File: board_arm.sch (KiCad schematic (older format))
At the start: 153 parts, among them SW1 SW_SPDT, U1 STM32F072CBT6, U2 PRTR5V0U2X, U3 MCP1725-3302E_SN

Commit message: Renumber the caps
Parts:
- renumbered C12 to C1, C1 to C3, C6 to C5, C7 to C6, C9 to C7, C10 to C8, C11 to C9
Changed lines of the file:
@@
 $EndDescr
 $Comp
-L Device:C_Small C1
+L Device:C_Small C3
 U 1 1 5C603E42
 P 1725 5275
-F 0 "C1" H 1817 5321 50  0000 L CNN
+F 0 "C3" H 1817 5321 50  0000 L CNN
 F 1 "0.1uF" H 1817 5230 50  0000 L CNN
 F 2 "Capacitor_SMD:C_0805_2012Metric" H 1725 5275 50  0001 C CNN
@@
 $EndComp
 $Comp
-L Device:C_Small C11
+L Device:C_Small C9
 U 1 1 5C9712E3
 P 7575 7200
-F 0 "C11" H 7667 7246 50  0000 L CNN
+F 0 "C9" H 7667 7246 50  0000 L CNN
 F 1 "10uF" H 7667 7155 50  0000 L CNN
 F 2 "Capacitor_SMD:C_0805_2012Metric" H 7575 7200 50  0001 C CNN
@@
 	5650 6700 5650 6600
 $Comp
-L Device:C_Small C9
+L Device:C_Small C7
 U 1 1 5CA16B93
 P 5425 6750
-F 0 "C9" H 5517 6796 50  0000 L CNN
+F 0 "C7" H 5517 6796 50  0000 L CNN
 F 1 "10uF" H 5517 6705 50  0000 L CNN
 F 2 "Capacitor_SMD:C_0805_2012Metric" H 5425 6750 50  0001 C CNN
@@
 	7950 6600 7950 6525
 $Comp
-L Device:C_Small C10
+L Device:C_Small C8
 U 1 1 5CA47771
 P 7150 7200
-F 0 "C10" H 7242 7246 50  0000 L CNN
+F 0 "C8" H 7242 7246 50  0000 L CNN
 F 1 "1nF" H 7242 7155 50  0000 L CNN
 F 2 "Capacitor_SMD:C_0805_2012Metric" H 7150 7200 50  0001 C CNN
@@
 PWRGD
 $Comp
-L Device:C_Small C6
+L Device:C_Small C5
 U 1 1 5D2621C9
 P 2525 5275
-F 0 "C6" H 2617 5321 50  0000 L CNN
+F 0 "C5" H 2617 5321 50  0000 L CNN
 F 1 "4.7uF" H 2617 5230 50  0000 L CNN
 F 2 "Capacitor_SMD:C_0805_2012Metric" H 2525 5275 50  0001 C CNN
@@
 $EndComp
 $Comp
-L Device:C_Small C7
+L Device:C_Small C6
 U 1 1 5D29FD29
 P 2925 5275
-F 0 "C7" H 3017 5321 50  0000 L CNN
+F 0 "C6" H 3017 5321 50  0000 L CNN
 F 1 "10nF" H 3017 5230 50  0000 L CNN
 F 2 "Capacitor_SMD:C_0805_2012Metric" H 2925 5275 50  0001 C CNN
@@
 NoConn ~ 2425 2625
 $Comp
-L Device:C_Small C12
+L Device:C_Small C1
 U 1 1 5C774367
 P 1950 1575
-F 0 "C12" H 2042 1621 50  0000 L CNN
+F 0 "C1" H 2042 1621 50  0000 L CNN
 F 1 "0.1uF" H 2042 1530 50  0000 L CNN
 F 2 "Capacitor_SMD:C_0805_2012Metric" H 1950 1575 50  0001 C CNN

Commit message: routage premiere version
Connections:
- net COL0: now also K_CAPS1.1 (COL), K_ESC1.1 (COL), K_SHIFT1.1 (COL), K_TAB1.1 (COL), U1.28 (PB15)
- net COL1: now also K_#1.1 (COL), K_A1.1 (COL), K_Q1.1 (COL), U1.27 (PB14)
- net COL10: now also K_#10.1 (COL), K_.1.1 (COL), K_;1.1 (COL), K_P1.1 (COL), U1.43 (PB7)
- net COL11: now also K_'1.1 (COL), K_-1.1 (COL), K_/1.1 (COL), K_[1.1 (COL), U1.42 (PB6)
- net COL12: now also K_=1.1 (COL), K_RSHIFT1.1 (COL), K_]1.1 (COL), U1.41 (PB5)
- net COL13: now also K_BACK1.1 (COL), K_ENTER1.1 (COL), K_\1.1 (COL), U1.39 (PB3)
- net COL14: now also K_UP1.1 (COL), U1.40 (PB4)
- net COL15: now also K_DELETE1.1 (COL), K_INSERT1.1 (COL), U1.18 (PB0)
- net COL2: now also K_#2.1 (COL), K_S1.1 (COL), K_W1.1 (COL), K_Z1.1 (COL), U1.26 (PB13)
- net COL3: now also K_#3.1 (COL), K_D1.1 (COL), K_E1.1 (COL), U1.25 (PB12)
- net COL4: now also K_#4.1 (COL), K_F1.1 (COL), K_R1.1 (COL), U1.22 (PB11)
- net COL5: now also K_#5.1 (COL), K_G1.1 (COL), K_T1.1 (COL), U1.21 (PB10)
- net COL6: now also K_#6.1 (COL), K_B1.1 (COL), K_H1.1 (COL), K_Y1.1 (COL), U1.20 (PB2)
- net COL7: now also K_#7.1 (COL), K_J1.1 (COL), K_U1.1 (COL), U1.19 (PB1)
- net COL8: now also K_#8.1 (COL), K_I1.1 (COL), K_K1.1 (COL), U1.46 (PB9)
- net COL9: now also K_#9.1 (COL), K_L1.1 (COL), K_O1.1 (COL), U1.45 (PB8)
- net ROW0: now also U1.13 (PA3)
- net ROW1: now also U1.14 (PA4)
- net ROW2: now also U1.15 (PA5)
- net ROW3: now also U1.10 (PA0)
- net ROW4: now also U1.11 (PA1)
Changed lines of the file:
@@
 Connection ~ 7150 6600
 Wire Wire Line
-	13975 2050 13975 4775
-Wire Wire Line
-	14575 2050 14575 4775
-Wire Wire Line
-	13375 2050 13375 4775
-Wire Wire Line
-	12775 2050 12775 4775
-Wire Wire Line
-	12175 2050 12175 4775
-Wire Wire Line
-	11575 2050 11575 4775
-Wire Wire Line
-	10975 2050 10975 4125
-Wire Wire Line
-	10375 2050 10375 4125
-Wire Wire Line
-	9775 2050 9775 4125
-Wire Wire Line
-	8575 2050 8575 4125
-Wire Wire Line
-	7975 2050 7975 4125
-Wire Wire Line
-	7375 2050 7375 4125
-Wire Wire Line
-	6775 2050 6775 4775
-Wire Wire Line
-	6175 2050 6175 4775
-Wire Wire Line
-	5575 2050 5575 4775
-Wire Wire Line
-	9175 2050 9175 4775
+	13975 2050 13975 4125
+Wire Wire Line
+	14575 2050 14575 2175
+Wire Wire Line
+	13375 2050 13375 2175
+Wire Wire Line
+	12775 2050 12775 2175
+Wire Wire Line
+	12175 2050 12175 2175
+Wire Wire Line
+	11575 2050 11575 2175
+Wire Wire Line
+	10975 2050 10975 2175
+Wire Wire Line
+	10375 2050 10375 2175
+Wire Wire Line
+	9775 2050 9775 2175
+Wire Wire Line
+	8575 2050 8575 2175
+Wire Wire Line
+	7975 2050 7975 2175
+Wire Wire Line
+	7375 2050 7375 2175
+Wire Wire Line
+	6775 2050 6775 2175
+Wire Wire Line
+	6175 2050 6175 2175
+Wire Wire Line
+	5575 2050 5575 2175
+Wire Wire Line
+	9175 2050 9175 2175
 $Comp
 L Connector:TestPoint TP1
@@
 Connection ~ 3125 4550
 $Comp
-L power:GND #PWR?
+L power:GND #PWR0110
 U 1 1 5D08B550
 P 2650 4550
-F 0 "#PWR?" H 2650 4300 50  0001 C CNN
+F 0 "#PWR0110" H 2650 4300 50  0001 C CNN
 F 1 "GND" H 2655 4377 50  0000 C CNN
 F 2 "" H 2650 4550 50  0001 C CNN
@@
 $EndComp
 $Comp
-L power:GND #PWR?
+L power:GND #PWR0116
 U 1 1 5C775F80
 P 1950 1675
-F 0 "#PWR?" H 1950 1425 50  0001 C CNN
+F 0 "#PWR0116" H 1950 1425 50  0001 C CNN
 F 1 "GND" H 1955 1502 50  0000 C CNN
 F 2 "" H 1950 1675 50  0001 C CNN
@@
 Wire Wire Line
 	2650 4550 2925 4550
+Text GLabel 2425 2825 0    50   Input ~ 0
+COL15
+Text GLabel 2425 2925 0    50   Input ~ 0
+COL7
+Text GLabel 2425 3025 0    50   Input ~ 0
+COL6
+Text GLabel 2425 3125 0    50   Input ~ 0
+COL13
+Text GLabel 2425 3225 0    50   Input ~ 0
+COL14
+Text GLabel 2425 3325 0    50   Input ~ 0
+COL12
+Text GLabel 2425 3425 0    50   Input ~ 0
+COL11
+Text GLabel 2425 3525 0    50   Input ~ 0
+COL10
+Text GLabel 2425 3625 0    50   Input ~ 0
+COL9
+Text GLabel 2425 3725 0    50   Input ~ 0
+COL8
+Text GLabel 2425 3825 0    50   Input ~ 0
+COL5
+Text GLabel 2425 3925 0    50   Input ~ 0
+COL4
+Text GLabel 2425 4025 0    50   Input ~ 0
+COL3
+Text GLabel 2425 4125 0    50   Input ~ 0
+COL2
+Text GLabel 2425 4225 0    50   Input ~ 0
+COL1
+Text GLabel 2425 4325 0    50   Input ~ 0
+COL0
+Text GLabel 3725 3125 2    50   Input ~ 0
+ROW0
+Text GLabel 3725 3225 2    50   Input ~ 0
+ROW1
+Text GLabel 3725 3325 2    50   Input ~ 0
+ROW2
+Text GLabel 3725 2825 2    50   Input ~ 0
+ROW3
+Text GLabel 3725 2925 2    50   Input ~ 0
+ROW4
+Connection ~ 13975 4125
+Wire Wire Line
+	13975 4125 13975 4775
+Connection ~ 12775 4125
+Wire Wire Line
+	12775 4125 12775 4775
+Connection ~ 12175 4125
+Wire Wire Line
+	12175 4125 12175 4775
+Connection ~ 11575 4125
+Wire Wire Line
+	11575 4125 11575 4775
+Connection ~ 11575 3475
+Wire Wire Line
+	11575 3475 11575 4125
+Connection ~ 12175 3475
+Wire Wire Line
+	12175 3475 12175 4125
+Connection ~ 9775 3475
+Wire Wire Line
+	9775 3475 9775 4125
+Connection ~ 10375 3475
+Wire Wire Line
+	10375 3475 10375 4125
+Connection ~ 10375 2825
+Wire Wire Line
+	10375 2825 10375 3475
+Connection ~ 9775 2825
+Wire Wire Line
+	9775 2825 9775 3475
+Connection ~ 9175 4125
+Wire Wire Line
+	9175 4125 9175 4775
+Connection ~ 9175 3475
+Wire Wire Line
+	9175 3475 9175 4125
+Connection ~ 9175 2825
+Wire Wire Line
+	9175 2825 9175 3475
+Connection ~ 9775 2175
+Wire Wire Line
+	9775 2175 9775 2825
+Connection ~ 9175 2175
+Wire Wire Line
+	9175 2175 9175 2825
+Connection ~ 10375 2175
+Wire Wire Line
+	10375 2175 10375 2825
+Connection ~ 10975 2175
+Wire Wire Line
+	10975 2175 10975 2825
+Connection ~ 11575 2175
+Wire Wire Line
+	11575 2175 11575 2825
+Connection ~ 12175 2175
+Wire Wire Line
+	12175 2175 12175 2825
+Connection ~ 12775 2175
+Wire Wire Line
+	12775 2175 12775 2825
+Connection ~ 13375 2175
+Wire Wire Line
+	13375 2175 13375 2825
+Connection ~ 14575 2175
+Wire Wire Line
+	14575 2175 14575 2825
+Connection ~ 14575 2825
+Wire Wire Line
+	14575 2825 14575 4775
+Connection ~ 13375 3475
+Wire Wire Line
+	13375 3475 13375 4775
+Connection ~ 13375 2825
+Wire Wire Line
+	13375 2825 13375 3475
+Connection ~ 12775 2825
+Wire Wire Line
+	12775 2825 12775 4125
+Connection ~ 12175 2825
+Wire Wire Line
+	12175 2825 12175 3475
+Connection ~ 11575 2825
+Wire Wire Line
+	11575 2825 11575 3475
+Connection ~ 10975 2825
+Wire Wire Line
+	10975 2825 10975 3475
+Connection ~ 10975 3475
+Wire Wire Line
+	10975 3475 10975 4125
+Connection ~ 6775 4125
+Wire Wire Line
+	6775 4125 6775 4775
+Connection ~ 5575 4125
+Wire Wire Line
+	5575 4125 5575 4775
+Connection ~ 5575 3475
+Wire Wire Line
+	5575 3475 5575 4125
+Connection ~ 6175 3475
+Wire Wire Line
+	6175 3475 6175 4775
+Connection ~ 6775 3475
+Wire Wire Line
+	6775 3475 6775 4125
+Connection ~ 7375 3475
+Wire Wire Line
+	7375 3475 7375 4125
+Connection ~ 8575 3475
+Wire Wire Line
+	8575 3475 8575 4125
+Connection ~ 7975 3475
+Wire Wire Line
+	7975 3475 7975 4125
+Connection ~ 6775 2825
+Wire Wire Line
+	6775 2825 6775 3475
+Connection ~ 6175 2825
+Wire Wire Line
+	6175 2825 6175 3475
+Connection ~ 5575 2825
+Wire Wire Line
+	5575 2825 5575 3475
+Connection ~ 7375 2825
+Wire Wire Line
+	7375 2825 7375 3475
+Connection ~ 7975 2825
+Wire Wire Line
+	7975 2825 7975 3475
+Connection ~ 8575 2825
+Wire Wire Line
+	8575 2825 8575 3475
+Connection ~ 8575 2175
+Wire Wire Line
+	8575 2175 8575 2825
+Connection ~ 7975 2175
+Wire Wire Line
+	7975 2175 7975 2825
+Connection ~ 7375 2175
+Wire Wire Line
+	7375 2175 7375 2825
+Connection ~ 6775 2175
+Wire Wire Line
+	6775 2175 6775 2825
+Connection ~ 6175 2175
+Wire Wire Line
+	6175 2175 6175 2825
+Connection ~ 5575 2175
+Wire Wire Line
+	5575 2175 5575 2825
 $EndSCHEMATC

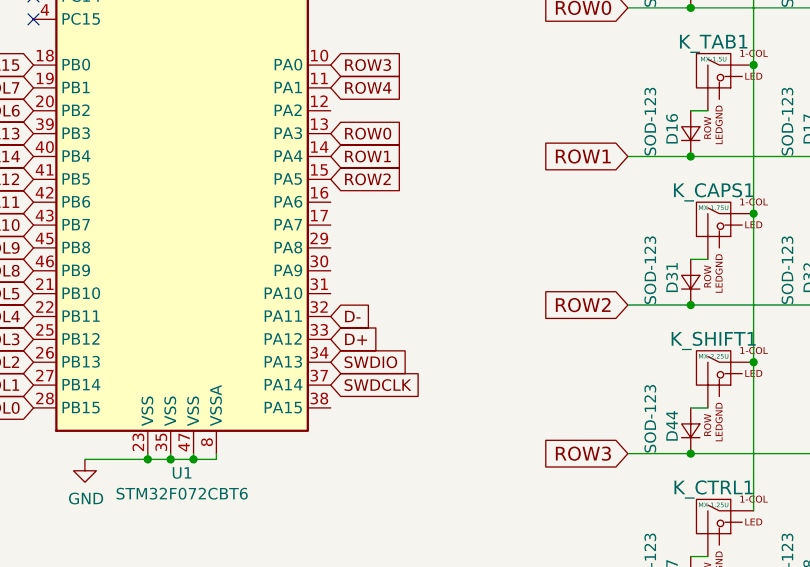
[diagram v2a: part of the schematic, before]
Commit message: deplacement switch, ajout LED, correction DRC
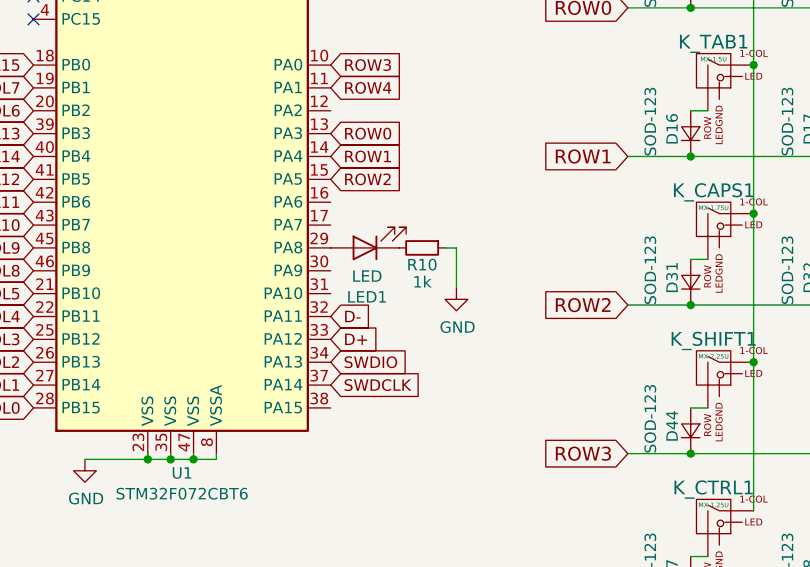
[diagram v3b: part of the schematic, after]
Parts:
- added LED1: LED, LED_SMD:LED_0805_2012Metric, symbol Device:LED
- added R10: 1k, Resistor_SMD:R_0805_2012Metric, symbol Device:R_Small
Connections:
- net GND: now also R10.1
- net at U1.29 (PA8): now also LED1.2 (A)
- new net: LED1.1 (K), R10.2
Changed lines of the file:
@@
 Wire Wire Line
 	5575 2175 5575 2825
+$Comp
+L Device:R_Small R?
+U 1 1 5C845B2F
+P 4125 3625
+AR Path="/5C70FC4F/5C845B2F" Ref="R?"  Part="1"
+AR Path="/5C845B2F" Ref="R10"  Part="1"
+F 0 "R10" V 4200 3625 50  0000 C CNN
+F 1 "1k" V 4275 3625 50  0000 C CNN
+F 2 "Resistor_SMD:R_0805_2012Metric" H 4125 3625 50  0001 C CNN
+F 3 "~" H 4125 3625 50  0001 C CNN
+	1    4125 3625
+	0    1    1    0
+$EndComp
+$Comp
+L Device:LED LED1
+U 1 1 5C8613BE
+P 3875 3625
+F 0 "LED1" H 3866 3841 50  0000 C CNN
+F 1 "LED" H 3866 3750 50  0000 C CNN
+F 2 "LED_SMD:LED_0805_2012Metric" H 3875 3625 50  0001 C CNN
+F 3 "~" H 3875 3625 50  0001 C CNN
+	1    3875 3625
+	-1   0    0    1
+$EndComp
+$Comp
+L power:GND #PWR?
+U 1 1 5C976169
+P 4275 3800
+F 0 "#PWR?" H 4275 3550 50  0001 C CNN
+F 1 "GND" H 4280 3627 50  0000 C CNN
+F 2 "" H 4275 3800 50  0001 C CNN
+F 3 "" H 4275 3800 50  0001 C CNN
+	1    4275 3800
+	1    0    0    -1
+$EndComp
+Wire Wire Line
+	4275 3800 4275 3625
+Wire Wire Line
+	4275 3625 4225 3625
 $EndSCHEMATC

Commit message: Cleanups
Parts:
- K_#1, K_#10, K_#2, K_#3, K_#4, K_#5, K_#6, K_#7, K_#8, K_#9, K_'1, K_,1, K_-1, K_.1, K_/1, K_;1, K_=1, K_A1, K_ALT1, K_B1, K_BACK1, K_C1, K_CAPS1, K_CTRL1, K_D1, K_DELETE1, K_DOWN1, K_E1, K_ENTER1, K_ESC1, K_F1, K_FN1, K_G1, K_H1, K_I1, K_INSERT1, K_J1, K_K1, K_L1, K_LEFT1, K_M1, K_N1, K_O1, K_P1, K_Q1, K_R1, K_RALT1, K_RCTRL1, K_RIGHT1, K_RSHIFT1, K_S1, K_SHIFT1, K_SPACE1, K_T1, K_TAB1, K_U1, K_UP1, K_V1, K_W1, K_WIN1, K_X1, K_Y1, K_Z1, K_[1, K_]1: symbol board_arm-rescue:MX-1U-MX_Alps_Hybrids -> MX_Alps_Hybrids:MX-1U
- K_\1: symbol board_arm-rescue:MX-1.5U-MX_Alps_Hybrids -> MX_Alps_Hybrids:MX-1.5U
- USB1: symbol board_arm-rescue:HRO-TYPE-C-31-M-12-Type-C -> Type-C:HRO-TYPE-C-31-M-12
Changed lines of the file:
@@
 encoding utf-8
 Sheet 1 1
-Title "FC660M Édition Gaulois"
+Title "FC660M AT-AT"
 Date ""
 Rev ""
@@
 $EndComp
 $Comp
-L board_arm-rescue:HRO-TYPE-C-31-M-12-Type-C USB?
+L Type-C:HRO-TYPE-C-31-M-12 USB?
 U 1 1 5C8D49E5
 P 1325 6600
@@
 $EndComp
 $Comp
-L board_arm-rescue:MX-1U-MX_Alps_Hybrids K_#1
+L MX_Alps_Hybrids:MX-1U K_#1
 U 1 1 5C9939AB
 P 6000 2200
@@
 $EndComp
 $Comp
-L board_arm-rescue:MX-1U-MX_Alps_Hybrids K_#2
+L MX_Alps_Hybrids:MX-1U K_#2
 U 1 1 5C9939C0
 P 6600 2200
@@
 $EndComp
 $Comp
-L board_arm-rescue:MX-1U-MX_Alps_Hybrids K_#3
+L MX_Alps_Hybrids:MX-1U K_#3
 U 1 1 5C9939D5
 P 7200 2200
@@
 $EndComp
 $Comp
-L board_arm-rescue:MX-1U-MX_Alps_Hybrids K_#4
+L MX_Alps_Hybrids:MX-1U K_#4
 U 1 1 5C9939EA
 P 7800 2200
@@
 $EndComp
 $Comp
-L board_arm-rescue:MX-1U-MX_Alps_Hybrids K_#5
+L MX_Alps_Hybrids:MX-1U K_#5
 U 1 1 5C9939FF
 P 8400 2200
@@
 $EndComp
 $Comp
-L board_arm-rescue:MX-1U-MX_Alps_Hybrids K_#6
+L MX_Alps_Hybrids:MX-1U K_#6
 U 1 1 5C993A14
 P 9000 2200
@@
 $EndComp
 $Comp
-L board_arm-rescue:MX-1U-MX_Alps_Hybrids K_#7
+L MX_Alps_Hybrids:MX-1U K_#7
 U 1 1 5C993A29
 P 9600 2200
@@
 $EndComp
 $Comp
-L board_arm-rescue:MX-1U-MX_Alps_Hybrids K_#8
+L MX_Alps_Hybrids:MX-1U K_#8
 U 1 1 5C993A3E
 P 10200 2200
@@
 $EndComp
 $Comp
-L board_arm-rescue:MX-1U-MX_Alps_Hybrids K_#9
+L MX_Alps_Hybrids:MX-1U K_#9
 U 1 1 5C993A53
 P 10800 2200
@@
 $EndComp
 $Comp
-L board_arm-rescue:MX-1U-MX_Alps_Hybrids K_#10
+L MX_Alps_Hybrids:MX-1U K_#10
 U 1 1 5C993A68
 P 11400 2200
@@
 $EndComp
 $Comp
-L board_arm-rescue:MX-1U-MX_Alps_Hybrids K_-1
+L MX_Alps_Hybrids:MX-1U K_-1
 U 1 1 5C993A7D
 P 12000 2200
@@
 $EndComp
 $Comp
-L board_arm-rescue:MX-1U-MX_Alps_Hybrids K_=1
+L MX_Alps_Hybrids:MX-1U K_=1
 U 1 1 5C993A92
 P 12600 2200
@@
 $EndComp
 $Comp
-L board_arm-rescue:MX-1U-MX_Alps_Hybrids K_BACK1
+L MX_Alps_Hybrids:MX-1U K_BACK1
 U 1 1 5C993AA7
 P 13200 2200
@@
 $EndComp
 $Comp
-L board_arm-rescue:MX-1U-MX_Alps_Hybrids K_TAB1
+L MX_Alps_Hybrids:MX-1U K_TAB1
 U 1 1 5C993ABC
 P 5400 2850
@@
 $EndComp
 $Comp
-L board_arm-rescue:MX-1U-MX_Alps_Hybrids K_W1
+L MX_Alps_Hybrids:MX-1U K_W1
 U 1 1 5C993AE6
 P 6600 2850
@@
 $EndComp
 $Comp
-L board_arm-rescue:MX-1U-MX_Alps_Hybrids K_E1
+L MX_Alps_Hybrids:MX-1U K_E1
 U 1 1 5C993AFB
 P 7200 2850
@@
 $EndComp
 $Comp
-L board_arm-rescue:MX-1U-MX_Alps_Hybrids K_R1
+L MX_Alps_Hybrids:MX-1U K_R1
 U 1 1 5C993B10
 P 7800 2850
@@
 $EndComp
 $Comp
-L board_arm-rescue:MX-1U-MX_Alps_Hybrids K_T1
+L MX_Alps_Hybrids:MX-1U K_T1
 U 1 1 5C993B25
 P 8400 2850
@@
 $EndComp
 $Comp
-L board_arm-rescue:MX-1U-MX_Alps_Hybrids K_Y1
+L MX_Alps_Hybrids:MX-1U K_Y1
 U 1 1 5C993B3A
 P 9000 2850
@@
 $EndComp
 $Comp
-L board_arm-rescue:MX-1U-MX_Alps_Hybrids K_I1
+L MX_Alps_Hybrids:MX-1U K_I1
 U 1 1 5C993B64
 P 10200 2850
@@
 $EndComp
 $Comp
-L board_arm-rescue:MX-1U-MX_Alps_Hybrids K_O1
+L MX_Alps_Hybrids:MX-1U K_O1
 U 1 1 5C993B79
 P 10800 2850
@@
 $EndComp
 $Comp
-L board_arm-rescue:MX-1U-MX_Alps_Hybrids K_P1
+L MX_Alps_Hybrids:MX-1U K_P1
 U 1 1 5C993B8E
 P 11400 2850
@@
 $EndComp
 $Comp
-L board_arm-rescue:MX-1U-MX_Alps_Hybrids K_[1
+L MX_Alps_Hybrids:MX-1U K_[1
 U 1 1 5C993BA3
 P 12000 2850
@@
 $EndComp
 $Comp
-L board_arm-rescue:MX-1U-MX_Alps_Hybrids K_]1
+L MX_Alps_Hybrids:MX-1U K_]1
 U 1 1 5C993BB8
 P 12600 2850
@@
 $EndComp
 $Comp
-L board_arm-rescue:MX-1.5U-MX_Alps_Hybrids K_\1
+L MX_Alps_Hybrids:MX-1.5U K_\1
 U 1 1 5C993BCD
 P 13200 2850
@@
 $EndComp
 $Comp
-L board_arm-rescue:MX-1U-MX_Alps_Hybrids K_CAPS1
+L MX_Alps_Hybrids:MX-1U K_CAPS1
 U 1 1 5C993BE2
 P 5400 3500
@@
 $EndComp
 $Comp
-L board_arm-rescue:MX-1U-MX_Alps_Hybrids K_A1
+L MX_Alps_Hybrids:MX-1U K_A1
 U 1 1 5C993BF7
 P 6000 3500
@@
 $EndComp
 $Comp
-L board_arm-rescue:MX-1U-MX_Alps_Hybrids K_S1
+L MX_Alps_Hybrids:MX-1U K_S1
 U 1 1 5C993C0C
 P 6600 3500
@@
 $EndComp
 $Comp
-L board_arm-rescue:MX-1U-MX_Alps_Hybrids K_D1
+L MX_Alps_Hybrids:MX-1U K_D1
 U 1 1 5C993C21
 P 7200 3500
@@
 $EndComp
 $Comp
-L board_arm-rescue:MX-1U-MX_Alps_Hybrids K_F1
+L MX_Alps_Hybrids:MX-1U K_F1
 U 1 1 5C993C36
 P 7800 3500
@@
 $EndComp
 $Comp
-L board_arm-rescue:MX-1U-MX_Alps_Hybrids K_G1
+L MX_Alps_Hybrids:MX-1U K_G1
 U 1 1 5C993C4B
 P 8400 3500
@@
 $EndComp
 $Comp
-L board_arm-rescue:MX-1U-MX_Alps_Hybrids K_H1
+L MX_Alps_Hybrids:MX-1U K_H1
 U 1 1 5C993C60
 P 9000 3500
@@
 $EndComp
 $Comp
-L board_arm-rescue:MX-1U-MX_Alps_Hybrids K_K1
+L MX_Alps_Hybrids:MX-1U K_K1
 U 1 1 5C993C8A
 P 10200 3500
@@
 $EndComp
 $Comp
-L board_arm-rescue:MX-1U-MX_Alps_Hybrids K_L1
+L MX_Alps_Hybrids:MX-1U K_L1
 U 1 1 5C993C9F
 P 10800 3500
@@
 $EndComp
 $Comp
-L board_arm-rescue:MX-1U-MX_Alps_Hybrids K_;1
+L MX_Alps_Hybrids:MX-1U K_;1
 U 1 1 5C993CB4
 P 11400 3500
@@
 $EndComp
 $Comp
-L board_arm-rescue:MX-1U-MX_Alps_Hybrids K_'1
+L MX_Alps_Hybrids:MX-1U K_'1
 U 1 1 5C993CC9
 P 12000 3500
@@
 $EndComp
 $Comp
-L board_arm-rescue:MX-1U-MX_Alps_Hybrids K_ENTER1
+L MX_Alps_Hybrids:MX-1U K_ENTER1
 U 1 1 5C993CDE
 P 13200 3500
@@
 $EndComp
 $Comp
-L board_arm-rescue:MX-1U-MX_Alps_Hybrids K_SHIFT1
+L MX_Alps_Hybrids:MX-1U K_SHIFT1
 U 1 1 5C993CF3
 P 5400 4150
@@
 $EndComp
 $Comp
-L board_arm-rescue:MX-1U-MX_Alps_Hybrids K_X1
+L MX_Alps_Hybrids:MX-1U K_X1
 U 1 1 5C993D1D
 P 7200 4150
@@
 $EndComp
 $Comp
-L board_arm-rescue:MX-1U-MX_Alps_Hybrids K_C1
+L MX_Alps_Hybrids:MX-1U K_C1
 U 1 1 5C993D32
 P 7800 4150
@@
 $EndComp
 $Comp
-L board_arm-rescue:MX-1U-MX_Alps_Hybrids K_V1
+L MX_Alps_Hybrids:MX-1U K_V1
 U 1 1 5C993D47
 P 8400 4150
@@
 $EndComp
 $Comp
-L board_arm-rescue:MX-1U-MX_Alps_Hybrids K_B1
+L MX_Alps_Hybrids:MX-1U K_B1
 U 1 1 5C993D5C
 P 9000 4150
@@
 $EndComp
 $Comp
-L board_arm-rescue:MX-1U-MX_Alps_Hybrids K_N1
+L MX_Alps_Hybrids:MX-1U K_N1
 U 1 1 5C993D71
 P 9600 4150
@@
 $EndComp
 $Comp
-L board_arm-rescue:MX-1U-MX_Alps_Hybrids K_M1
+L MX_Alps_Hybrids:MX-1U K_M1
 U 1 1 5C993D86
 P 10200 4150
@@
 $EndComp
 $Comp
-L board_arm-rescue:MX-1U-MX_Alps_Hybrids K_,1
+L MX_Alps_Hybrids:MX-1U K_,1
 U 1 1 5C993D9B
 P 10800 4150
@@
 $EndComp
 $Comp
-L board_arm-rescue:MX-1U-MX_Alps_Hybrids K_.1
+L MX_Alps_Hybrids:MX-1U K_.1
 U 1 1 5C993DB0
 P 11400 4150
@@
 $EndComp
 $Comp
-L board_arm-rescue:MX-1U-MX_Alps_Hybrids K_RSHIFT1
+L MX_Alps_Hybrids:MX-1U K_RSHIFT1
 U 1 1 5C993DDA
 P 12600 4150
@@
 ROW4
 $Comp
-L board_arm-rescue:MX-1U-MX_Alps_Hybrids K_ALT1
+L MX_Alps_Hybrids:MX-1U K_ALT1
 U 1 1 5C993E8E
 P 6600 4800
@@
 $EndComp
 $Comp
-L board_arm-rescue:MX-1U-MX_Alps_Hybrids K_SPACE1
+L MX_Alps_Hybrids:MX-1U K_SPACE1
 U 1 1 5C993EB1
 P 9000 4800
@@
 Connection ~ 12500 5175
 $Comp
-L board_arm-rescue:MX-1U-MX_Alps_Hybrids K_RALT1
+L MX_Alps_Hybrids:MX-1U K_RALT1
 U 1 1 5C99416F
 P 11400 4800
@@
 $EndComp
 $Comp
-L board_arm-rescue:MX-1U-MX_Alps_Hybrids K_FN1
+L MX_Alps_Hybrids:MX-1U K_FN1
 U 1 1 5C994176
 P 12000 4800
@@
 $EndComp
 $Comp
-L board_arm-rescue:MX-1U-MX_Alps_Hybrids K_RCTRL1
+L MX_Alps_Hybrids:MX-1U K_RCTRL1
 U 1 1 5C994184
 P 12600 4800
@@
 Connection ~ 8900 5175
 $Comp
-L board_arm-rescue:MX-1U-MX_Alps_Hybrids K_ESC1
+L MX_Alps_Hybrids:MX-1U K_ESC1
 U 1 1 5C993996
 P 5400 2200
@@
 $EndComp
 $Comp
-L board_arm-rescue:MX-1U-MX_Alps_Hybrids K_Q1
+L MX_Alps_Hybrids:MX-1U K_Q1
 U 1 1 5C993AD1
 P 6000 2850
@@
 $EndComp
 $Comp
-L board_arm-rescue:MX-1U-MX_Alps_Hybrids K_CTRL1
+L MX_Alps_Hybrids:MX-1U K_CTRL1
 U 1 1 5C993E04
 P 5400 4800
@@
 $EndComp
 $Comp
-L board_arm-rescue:MX-1U-MX_Alps_Hybrids K_J1
+L MX_Alps_Hybrids:MX-1U K_J1
 U 1 1 5C993C75
 P 9600 3500
@@
 	12500 4325 12575 4325
 $Comp
-L board_arm-rescue:MX-1U-MX_Alps_Hybrids K_/1
+L MX_Alps_Hybrids:MX-1U K_/1
 U 1 1 5C993DC5
 P 12000 4150
@@
 	13100 3675 13175 3675
 $Comp
-L board_arm-rescue:MX-1U-MX_Alps_Hybrids K_U1
+L MX_Alps_Hybrids:MX-1U K_U1
 U 1 1 5C993B4F
 P 9600 2850
@@
 $EndComp
 $Comp
-L board_arm-rescue:MX-1U-MX_Alps_Hybrids K_Z1
+L MX_Alps_Hybrids:MX-1U K_Z1
 U 1 1 5C993D08
 P 6600 4150
@@
 $EndComp
 $Comp
-L board_arm-rescue:MX-1U-MX_Alps_Hybrids K_WIN1
+L MX_Alps_Hybrids:MX-1U K_WIN1
 U 1 1 5C993EAA
 P 6000 4800
@@
 	5300 4525 6500 4525
 $Comp
-L board_arm-rescue:MX-1U-MX_Alps_Hybrids K_LEFT1
+L MX_Alps_Hybrids:MX-1U K_LEFT1
 U 1 1 5F1D5B70
 P 13200 4800
@@
 	13700 4975 13775 4975
 $Comp
-L board_arm-rescue:MX-1U-MX_Alps_Hybrids K_DOWN1
+L MX_Alps_Hybrids:MX-1U K_DOWN1
 U 1 1 5F2A3A74
 P 13800 4800
@@
 	13700 4325 13775 4325
 $Comp
-L board_arm-rescue:MX-1U-MX_Alps_Hybrids K_UP1
+L MX_Alps_Hybrids:MX-1U K_UP1
 U 1 1 5F2F47D1
 P 13800 4150
@@
 	14300 4975 14375 4975
 $Comp
-L board_arm-rescue:MX-1U-MX_Alps_Hybrids K_RIGHT1
+L MX_Alps_Hybrids:MX-1U K_RIGHT1
 U 1 1 5F31BA81
 P 14400 4800
@@
 COL15
 $Comp
-L board_arm-rescue:MX-1U-MX_Alps_Hybrids K_INSERT1
+L MX_Alps_Hybrids:MX-1U K_INSERT1
 U 1 1 5F35AB42
 P 14400 2200
@@
 Connection ~ 13100 2575
 $Comp
-L board_arm-rescue:MX-1U-MX_Alps_Hybrids K_DELETE1
+L MX_Alps_Hybrids:MX-1U K_DELETE1
 U 1 1 5F38327F
 P 14400 2850
